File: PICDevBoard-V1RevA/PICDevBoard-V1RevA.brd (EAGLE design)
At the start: 100 x 60 mm, 15 parts, among them IC1 PIC18F2550, J1 DCJ0202

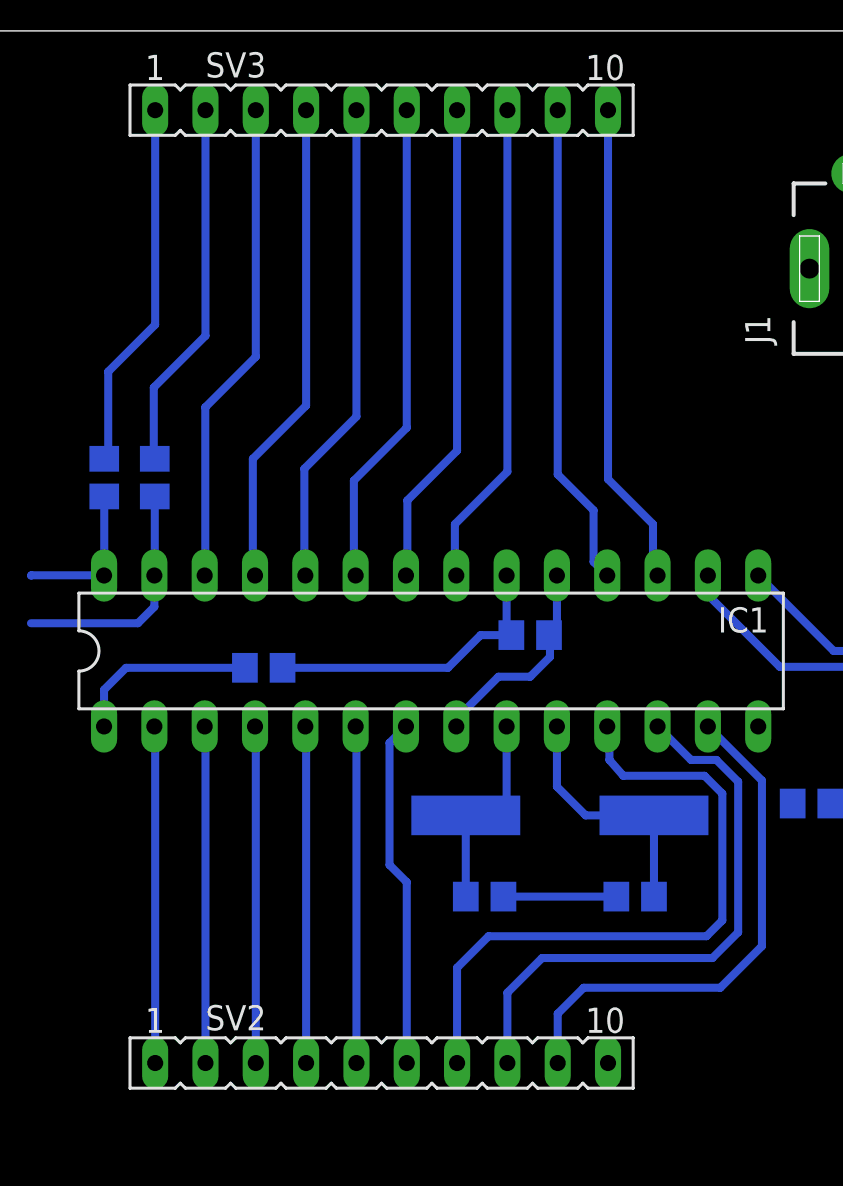
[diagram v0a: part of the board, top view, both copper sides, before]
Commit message: Silk
Adicionado nome dos pinos no silk (top layer)
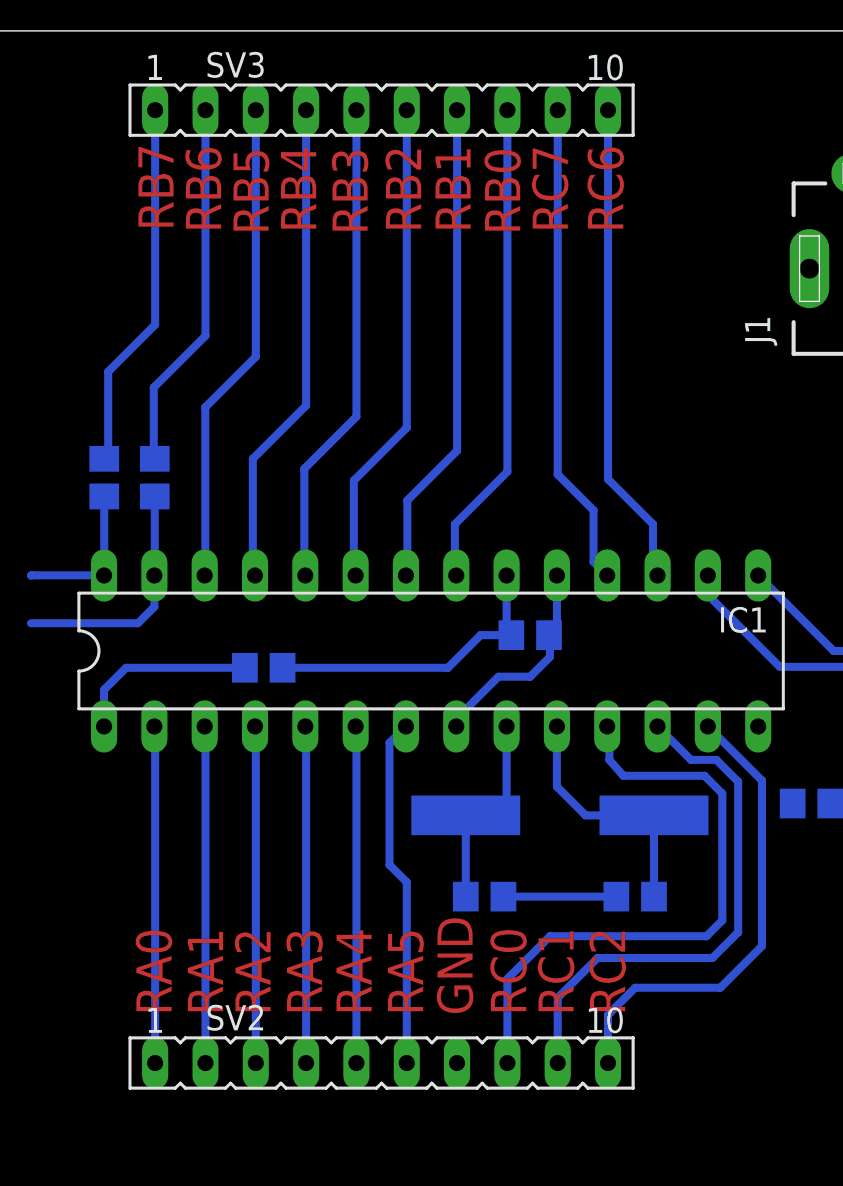
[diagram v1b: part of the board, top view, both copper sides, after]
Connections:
- net GND: now also SV2.7; no longer SV2.10
- net RC0: now also SV2.8; no longer SV2.7
- net RC1: now also SV2.9; no longer SV2.8
- net RC2: now also SV2.10; no longer SV2.9
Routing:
- net RC0: track 33.8 -> 30.9 mm
- net RC1: track 29.3 -> 26.6 mm
- net RC2: track 26.4 -> 23.9 mm
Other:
- board text added: "GND"
- board text added: "RA0"
- board text added: "RA1"
- board text added: "RA2"
- board text added: "RA3"
- board text added: "RA4"
- board text added: "RA5"
- board text added: "RB0"
- board text added: "RB1"
- board text added: "RB2"
- board text added: "RB3"
- board text added: "RB4"
- board text added: "RB5"
- board text added: "RB6"
- board text added: "RB7"
- board text added: "RC0"
- board text added: "RC1"
- board text added: "RC2"
- board text added: "RC6"
- board text added: "RC7"
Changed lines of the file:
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@@
 <?xml version="1.0" encoding="utf-8"?>
 <!DOCTYPE eagle SYSTEM "eagle.dtd">
-<eagle version="6.1">
+<eagle version="6.4">
 <drawing>
 <settings>
@@
 <wire x1="100" y1="60" x2="0" y2="60" width="0" layer="20"/>
 <wire x1="0" y1="60" x2="0" y2="0" width="0" layer="20"/>
-<dimension x1="100" y1="60" x2="0" y2="60" x3="50" y3="78.25" layer="1" dtype="horizontal"/>
-<dimension x1="0" y1="60" x2="0" y2="0" x3="-19.9" y3="30" layer="1" dtype="vertical"/>
+<dimension x1="100" y1="60" x2="0" y2="60" x3="50" y3="78.25" textsize="3.5" layer="1" dtype="horizontal"/>
+<dimension x1="0" y1="60" x2="0" y2="0" x3="-19.9" y3="30" textsize="3.5" layer="1" dtype="vertical"/>
 <text x="12.5" y="90.15" size="3.81" layer="1" font="vector" ratio="11">Tamanho fixo da placa</text>
 <hole x="3" y="3" drill="2.5"/>
@@
 <text x="104.5" y="30.4" size="1.778" layer="1">Nome dos pinos</text>
 <text x="103.9" y="26.8" size="1.778" layer="1">Pontos para "Sincronia"</text>
+<text x="36.7" y="10.3" size="1.778" layer="1" font="vector" ratio="11" rot="R90">RA0</text>
+<text x="39.3" y="10.3" size="1.778" layer="1" font="vector" ratio="11" rot="R90">RA1</text>
+<text x="41.7" y="10.3" size="1.778" layer="1" font="vector" ratio="11" rot="R90">RA2</text>
+<text x="44.3" y="10.3" size="1.778" layer="1" font="vector" ratio="11" rot="R90">RA3</text>
+<text x="46.8" y="10.3" size="1.778" layer="1" font="vector" ratio="11" rot="R90">RA4</text>
+<text x="49.4" y="10.3" size="1.778" layer="1" font="vector" ratio="11" rot="R90">RA5</text>
+<text x="51.9" y="10.3" size="1.778" layer="1" font="vector" ratio="11" rot="R90">GND</text>
+<text x="54.6" y="10.3" size="1.778" layer="1" font="vector" ratio="11" rot="R90">RC0</text>
+<text x="57" y="10.3" size="1.778" layer="1" font="vector" ratio="11" rot="R90">RC1</text>
+<text x="59.6" y="10.3" size="1.778" layer="1" font="vector" ratio="11" rot="R90">RC2</text>
+<text x="36.8" y="49.9" size="1.778" layer="1" font="vector" ratio="11" rot="R90">RB7</text>
+<text x="39.2" y="49.8" size="1.778" layer="1" font="vector" ratio="11" rot="R90">RB6</text>
+<text x="41.6" y="49.7" size="1.778" layer="1" font="vector" ratio="11" rot="R90">RB5</text>
+<text x="44" y="49.8" size="1.778" layer="1" font="vector" ratio="11" rot="R90">RB4</text>
+<text x="46.6" y="49.7" size="1.778" layer="1" font="vector" ratio="11" rot="R90">RB3</text>
+<text x="49.3" y="49.8" size="1.778" layer="1" font="vector" ratio="11" rot="R90">RB2</text>
+<text x="51.8" y="49.8" size="1.778" layer="1" font="vector" ratio="11" rot="R90">RB1</text>
+<text x="54.3" y="49.7" size="1.778" layer="1" font="vector" ratio="11" rot="R90">RB0</text>
+<text x="56.7" y="49.8" size="1.778" layer="1" font="vector" ratio="11" rot="R90">RC7</text>
+<text x="59.5" y="49.8" size="1.778" layer="1" font="vector" ratio="11" rot="R90">RC6</text>
 </plain>
 <attributes>
@@
 </class>
 </classes>
-<designrules>
+<designrules name="default">
 <description language="de">&lt;b&gt;EAGLE Design Rules&lt;/b&gt;
 &lt;p&gt;
@@
 <contactref element="C3" pad="2"/>
 <contactref element="USB1" pad="P$5"/>
-<contactref element="SV2" pad="10"/>
 <wire x1="53.45" y1="16.3" x2="59.15" y2="16.3" width="0.4064" layer="16"/>
 <wire x1="56.15" y1="32.51" x2="56.15" y2="29.9" width="0.4064" layer="16"/>
@@
 <wire x1="55.8" y1="28.4" x2="55.8" y2="29.45" width="0.4064" layer="16"/>
 <wire x1="55.8" y1="29.45" x2="55.75" y2="29.5" width="0.4064" layer="16"/>
+<contactref element="SV2" pad="7"/>
 <wire x1="69.95" y1="21" x2="92.2" y2="26.3" width="0" layer="19" extent="16-16"/>
 <wire x1="59.15" y1="16.3" x2="69.95" y2="21" width="0" layer="19" extent="16-16"/>
-<wire x1="58.73" y1="7.9" x2="59.15" y2="16.3" width="0" layer="19" extent="16-16"/>
+<wire x1="51.11" y1="7.9" x2="53.45" y2="16.3" width="0" layer="19" extent="16-16"/>
 <wire x1="51.07" y1="24.89" x2="53.45" y2="16.3" width="0" layer="19" extent="16-16"/>
 <wire x1="68.9" y1="48" x2="56.15" y2="32.51" width="0" layer="19" extent="1-1"/>
@@
 <wire x1="33.3" y1="32.52" x2="29.62" y2="32.52" width="0.4064" layer="16"/>
 <wire x1="29.62" y1="32.52" x2="29.6" y2="32.5" width="0.4064" layer="16"/>
-<wire x1="29.6" y1="32.5" x2="20.55" y2="27.06" width="0" layer="19" extent="1-16"/>
+<wire x1="20.55" y1="27.06" x2="29.6" y2="32.5" width="0" layer="19" extent="16-16"/>
 </signal>
 <signal name="PGC">
@@
 <signal name="RC0">
 <contactref element="IC1" pad="11"/>
-<contactref element="SV2" pad="7"/>
-<wire x1="51.11" y1="7.9" x2="51.11" y2="12.71" width="0.4064" layer="16"/>
-<wire x1="51.11" y1="12.71" x2="52.7" y2="14.3" width="0.4064" layer="16"/>
-<wire x1="52.7" y1="14.3" x2="63.7" y2="14.3" width="0.4064" layer="16"/>
 <wire x1="63.7" y1="14.3" x2="64.5" y2="15.1" width="0.4064" layer="16"/>
 <wire x1="64.5" y1="15.1" x2="64.5" y2="21.5" width="0.4064" layer="16"/>
@@
 <wire x1="58.8" y1="23.2" x2="58.8" y2="24.78" width="0.4064" layer="16"/>
 <wire x1="58.8" y1="24.78" x2="58.69" y2="24.89" width="0.4064" layer="16"/>
+<contactref element="SV2" pad="8"/>
+<wire x1="53.65" y1="7.9" x2="53.65" y2="12.15" width="0.4064" layer="16"/>
+<wire x1="53.65" y1="12.15" x2="55.8" y2="14.3" width="0.4064" layer="16"/>
+<wire x1="55.8" y1="14.3" x2="63.7" y2="14.3" width="0.4064" layer="16"/>
 </signal>
 <signal name="RC1">
 <contactref element="IC1" pad="12"/>
-<contactref element="SV2" pad="8"/>
-<wire x1="53.65" y1="7.9" x2="53.65" y2="11.45" width="0.4064" layer="16"/>
-<wire x1="53.65" y1="11.45" x2="55.4" y2="13.2" width="0.4064" layer="16"/>
-<wire x1="55.4" y1="13.2" x2="64" y2="13.2" width="0.4064" layer="16"/>
 <wire x1="64" y1="13.2" x2="65.3" y2="14.5" width="0.4064" layer="16"/>
 <wire x1="65.3" y1="14.5" x2="65.3" y2="22.1" width="0.4064" layer="16"/>
@@
 <wire x1="64.2" y1="23.2" x2="62.92" y2="23.2" width="0.4064" layer="16"/>
 <wire x1="62.92" y1="23.2" x2="61.23" y2="24.89" width="0.4064" layer="16"/>
+<contactref element="SV2" pad="9"/>
+<wire x1="56.19" y1="7.9" x2="56.19" y2="11.19" width="0.4064" layer="16"/>
+<wire x1="56.19" y1="11.19" x2="58.2" y2="13.2" width="0.4064" layer="16"/>
+<wire x1="58.2" y1="13.2" x2="64" y2="13.2" width="0.4064" layer="16"/>
 </signal>
 <signal name="RC2">
 <contactref element="IC1" pad="13"/>
-<contactref element="SV2" pad="9"/>
-<wire x1="56.19" y1="7.9" x2="56.19" y2="10.39" width="0.4064" layer="16"/>
-<wire x1="56.19" y1="10.39" x2="57.5" y2="11.7" width="0.4064" layer="16"/>
-<wire x1="57.5" y1="11.7" x2="64.4" y2="11.7" width="0.4064" layer="16"/>
+<wire x1="60.1" y1="11.7" x2="64.4" y2="11.7" width="0.4064" layer="16"/>
 <wire x1="64.4" y1="11.7" x2="66.5" y2="13.8" width="0.4064" layer="16"/>
 <wire x1="66.5" y1="13.8" x2="66.5" y2="22.16" width="0.4064" layer="16"/>
 <wire x1="66.5" y1="22.16" x2="63.77" y2="24.89" width="0.4064" layer="16"/>
+<contactref element="SV2" pad="10"/>
+<wire x1="58.73" y1="7.9" x2="58.73" y2="10.33" width="0.4064" layer="16"/>
+<wire x1="58.73" y1="10.33" x2="60.1" y2="11.7" width="0.4064" layer="16"/>
 </signal>
 <signal name="RB0">

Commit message: Routing
Continuação do roteamento
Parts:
- added SV4, SV5: (no value), con-lstb:MA03-1
- moved J1 19.3 mm to (89.7, 40.2)
- moved SV3 16.3 mm to (60.7, 46.7)
- moved ICSP 15.4 mm to (36.0, 28.7)
- moved SV2 13.7 mm to (60.7, 10.7)
- moved C4 12.3 mm to (81.2, 22.8)
- moved SV1 11.7 mm to (93.3, 29.8)
- moved IC1 10.9 mm to (60.7, 28.7)
- moved R2 10.9 mm to (44.2, 37.5)
- moved R3 10.9 mm to (46.8, 37.5)
- moved USB1 10.2 mm to (94.8, 17.7)
- moved C3 9.73 mm to (64.5, 28.7), turned to 270 degrees
- moved C1 9.51 mm to (62.0, 15.9)
- moved XTAL1 9.51 mm to (65.8, 20.0)
- moved C2 9.51 mm to (69.6, 15.9)
- moved R1 2.01 mm to (41.1, 25.9), turned to 90 degrees
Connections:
- net 5VICSP: now also SV1.2; no longer SV1.6
- net 5VUSB: now also SV1.6; no longer SV1.2
- net GND: now also SV5.1, SV5.2, SV5.3, USB1.P$6, USB1.P$7, USB1.P$8, USB1.P$9
- net VCC: now also SV4.1, SV4.2, SV4.3
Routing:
- net GND: track 16.4 -> 204.5 mm
- net VCC: track 15.3 -> 112.8 mm
- net 5VICSP: track 0.00 -> 89.8 mm
- net 5VJACK: track 0.00 -> 22.5 mm
- net RA2: track 17.0 -> 0.00 mm
- net RA4: track 17.0 -> 0.00 mm
- net RA3: track 17.0 -> 0.00 mm
- net RA1: track 17.0 -> 0.00 mm
- net RA0: track 17.0 -> 0.00 mm
- net PGD: track 7.70 -> 20.6 mm
- net RC6: track 24.5 -> 14.2 mm
- net RC7: track 24.5 -> 14.2 mm
- net 5VUSB: track 0.00 -> 9.79 mm
- net RB0: track 24.6 -> 16.3 mm
- net RB5: track 24.6 -> 16.3 mm
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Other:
- board text added: "HI-PWR"
- board text added: "Verificar conector JACK"

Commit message: Routing
Continuação
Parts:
- moved SV5 40.7 mm to (43.0, 2.70)
- moved SV4 38.8 mm to (43.0, 38.7)
- moved C4 38.5 mm to (43.8, 13.8)
- moved J1 38.0 mm to (52.6, 32.1)
- moved USB1 37.6 mm to (57.8, 10.8)
- moved SV1 36.9 mm to (57.3, 21.9)
- moved C1 36.6 mm to (26.3, 7.90)
- moved C3 36.6 mm to (28.8, 20.7)
- moved IC1 36.6 mm to (25.0, 20.7)
- moved R2 36.6 mm to (8.50, 29.4)
- moved R3 36.6 mm to (11.1, 29.4)
- moved SV2 36.6 mm to (25.0, 2.70)
- moved SV3 36.6 mm to (25.0, 38.7)
- moved C2 36.6 mm to (33.9, 7.90)
- moved XTAL1 36.6 mm to (30.1, 12.0)
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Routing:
- net N$1: track 0.00 -> 43.8 mm
- net VCC: track 112.8 -> 86.6 mm
- net RA4: track 0.00 -> 16.2 mm
- net RA0: track 0.00 -> 16.1 mm
- net RA3: track 0.00 -> 15.3 mm
- net RA2: track 0.00 -> 15.3 mm
- net RA1: track 0.00 -> 15.2 mm
- net 5VICSP: track 89.8 -> 82.6 mm
- net GND: track 204.5 -> 209.5 mm
- net VPP: track 8.77 -> 13.6 mm
- net N$3: track 0.00 -> 3.90 mm
- net USB_D+: track 28.1 -> 24.4 mm
- net PGC: track 17.3 -> 13.8 mm
- net 5VJACK: track 22.5 -> 19.4 mm
- net USB_D-: track 24.9 -> 22.3 mm
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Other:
- board size 100 x 60 mm -> 63 x 42 mm
- board text added: "HIPWR"
- board text added: "ICSP"
- board text added: "JACK"
- board text added: "PIC18F2550"
- board text added: "USB"
- board text added: "VCC"
- board text removed: "2 Layer"
- board text removed: "HI-PWR"
- board text removed: "Nome dos pinos"
- board text removed: "Pontos para "Sincronia""
- board text removed: "Silk"
- board text removed: "Tamanho fixo da placa"

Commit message: Routing
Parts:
- added C5: 10u, rcl:C0805
- moved USB1 1.70 mm to (56.1, 10.8)
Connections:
- net 5VJACK: now also J1.1; no longer J1.2, J1.3
- net GND: now also C5.2, J1.3; no longer J1.1
- net VCC: now also C5.1
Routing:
- net N$1: track 43.8 -> 0.00 mm
- net GND: track 209.5 -> 191.1 mm
- net N$3: track 3.90 -> 0.00 mm
- net VCC: track 86.6 -> 88.8 mm
- net N$2: track 1.90 -> 0.00 mm
- net USB_D-: track 22.3 -> 20.6 mm
- net USB_D+: track 24.4 -> 22.7 mm
- net 5VUSB: track 9.06 -> 10.4 mm
- net 5VJACK: track 19.4 -> 18.4 mm
- added copper zone on layer 16, net GND
- added copper zone on layer 16, net VCC
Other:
- board text added: "5V"
- board text added: "HI-PWR"
- board text removed: "HIPWR"
- board text removed: "Verificar conector JACK"
